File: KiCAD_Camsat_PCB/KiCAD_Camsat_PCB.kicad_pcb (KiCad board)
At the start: 2 copper layers, 60 x 140 mm, 62 parts, among them J1 Barrel_Jack, J3 105017-0001, K1 HYC77-TF09-200, Q2 SS8050-G_C164885, Q9 SS8050-G_C164885, SW1 PTS645SH50SMTR92LFS, SW2 PTS645SH50SMTR92LFS, U1 ISM330DHCX, U10 BME280, U5 DHT11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

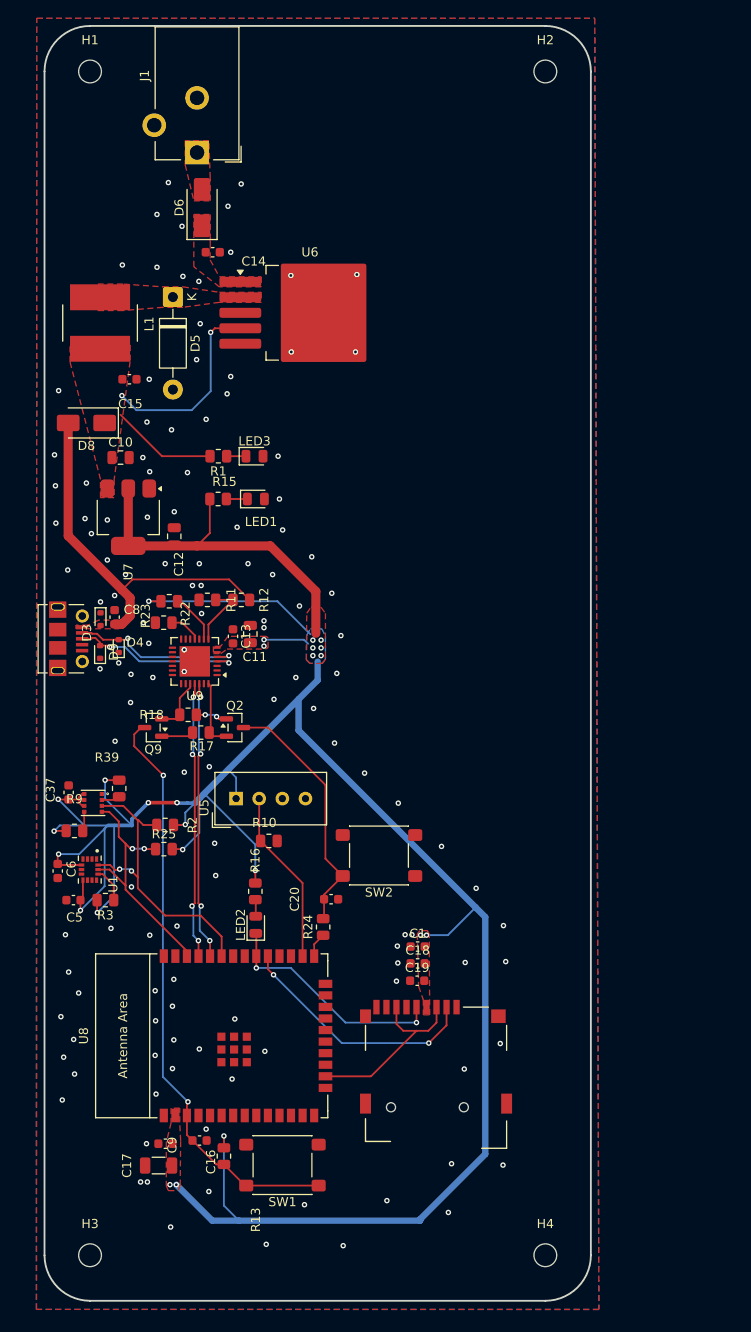
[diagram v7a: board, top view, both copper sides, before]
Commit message: PCB Board Updates
- Board Dimensions changed to  70mm width
- Descriptive Silkscreen values added
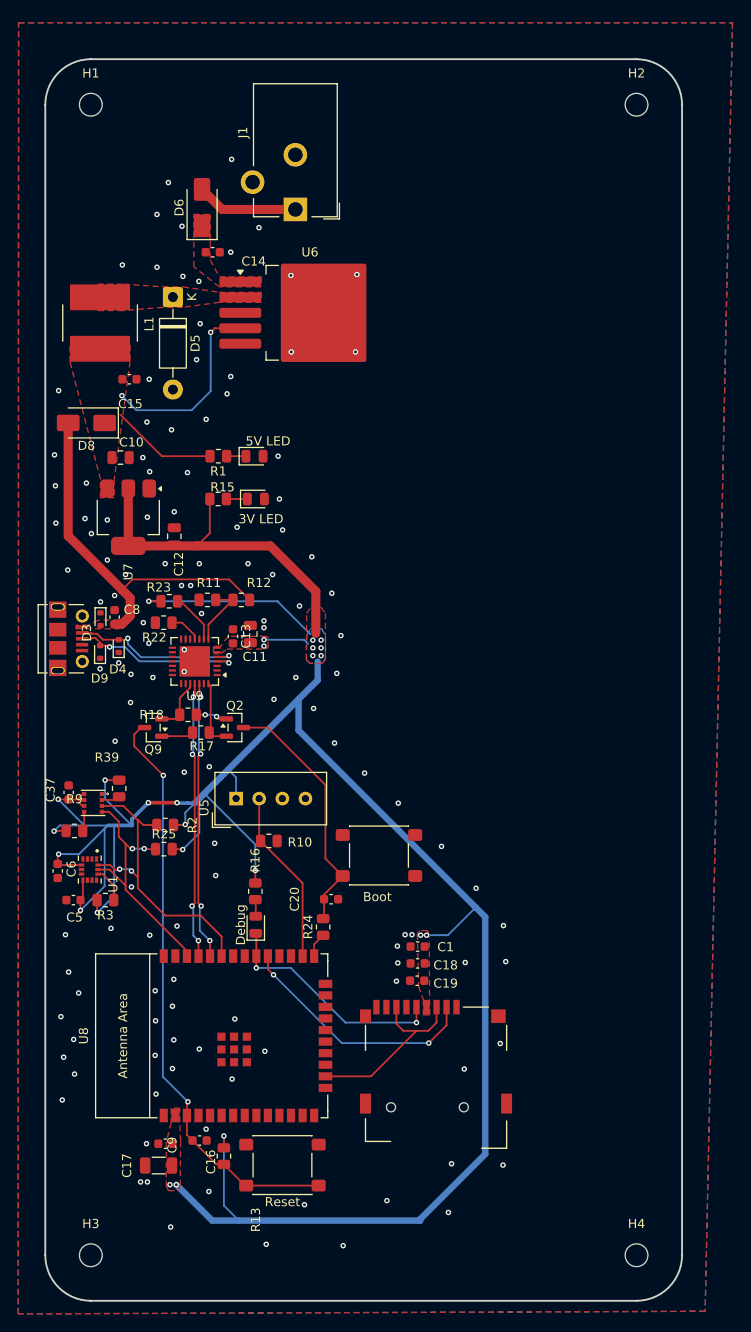
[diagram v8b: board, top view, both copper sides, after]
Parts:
- added G***: LOGO, esp32:silcatnobg, B.Cu at (101.6, 83.7)
- 3V LED: renamed from LED1
- 5V LED: renamed from LED3
- moved J1 12.5 mm to (79.0, 53.5)
- moved H2 10.7 mm to (116.5, 42.0)
- moved H4 10.0 mm to (116.5, 168.3)
- moved H1 3.65 mm to (56.5, 42.0)
- moved H3 0.09 mm to (56.5, 168.3)
- renumbered SW2 to Boot, LED2 to Debug, SW1 to Reset
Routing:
- net /9V: track 0.00 -> 11.2 mm
- removed copper zone on F.Cu, net /9V
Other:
- board size 60 x 140 mm -> 69.9 x 136.3 mm
